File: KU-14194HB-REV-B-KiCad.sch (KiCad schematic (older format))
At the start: 0 parts

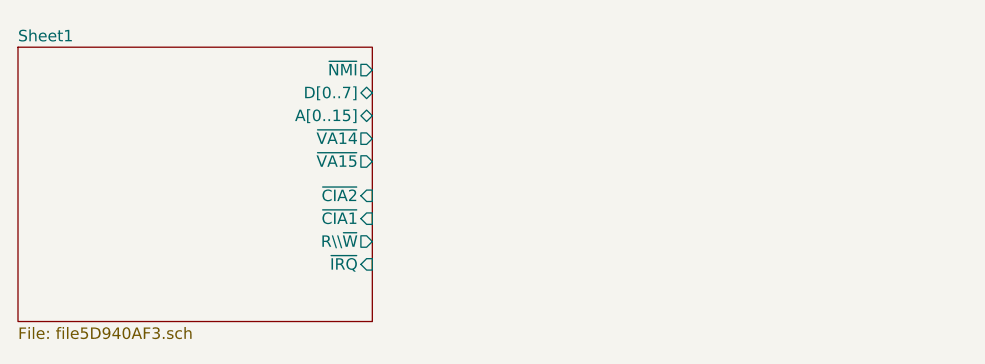
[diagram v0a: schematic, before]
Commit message: schematics update
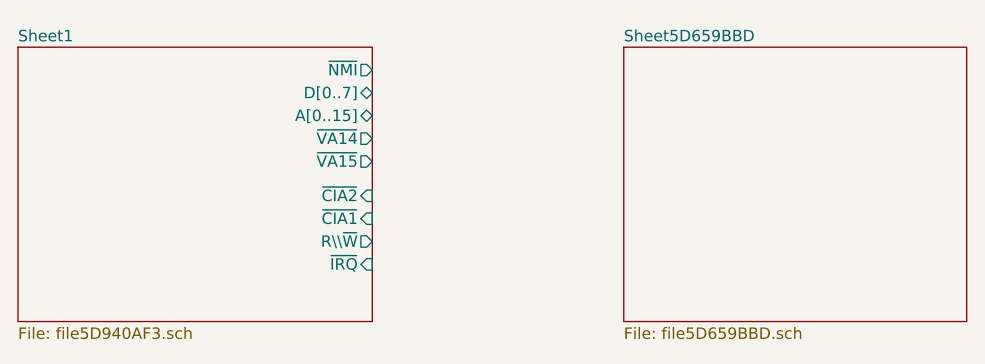
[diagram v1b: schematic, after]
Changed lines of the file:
@@
 $Descr A3 16535 11693
 encoding utf-8
-Sheet 1 2
+Sheet 1 3
 Title ""
 Date ""
@@
 F10 "~IRQ~" I R 4050 2450 50
 $EndSheet
+$Sheet
+S 5150 1500 1500 1200
+U 5D659BBE
+F0 "Sheet5D659BBD" 50
+F1 "file5D659BBD.sch" 50
+$EndSheet
 $EndSCHEMATC

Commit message: More schematics
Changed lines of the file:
@@
 F0 "Sheet5D659BBD" 50
 F1 "file5D659BBD.sch" 50
+F2 "D[0..7]" B L 5150 1700 39
 $EndSheet
+Wire Bus Line
+	5150 1700 4050 1700
+Text HLabel 4500 1700 1    39   Input ~ 0
+D[0..7]
 $EndSCHEMATC

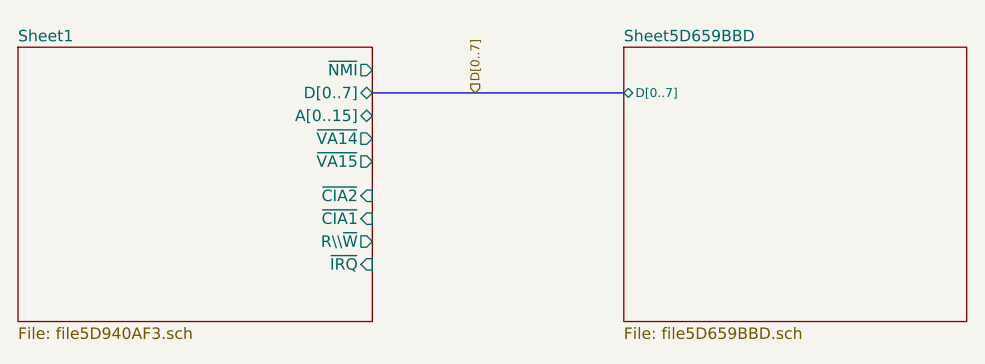
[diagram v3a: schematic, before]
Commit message: Schematics PDF and screenshot update
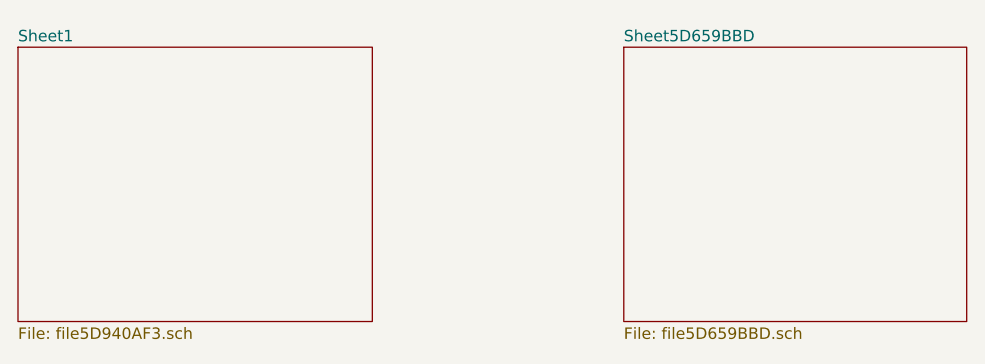
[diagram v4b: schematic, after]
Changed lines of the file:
@@
 encoding utf-8
 Sheet 1 3
-Title ""
-Date ""
+Title "C64 Motherboard KU-14194HB"
+Date "2019-09-28"
 Rev ""
-Comp ""
-Comment1 ""
+Comp "Commodore 1982"
+Comment1 "layout retraced and schematics drawn by bwack 2019"
 Comment2 ""
 Comment3 ""
@@
 F0 "Sheet1" 50
 F1 "file5D940AF3.sch" 50
-F2 "~NMI~" O R 4050 1600 50
-F3 "D[0..7]" B R 4050 1700 50
-F4 "A[0..15]" B R 4050 1800 50
-F5 "~VA14~" O R 4050 1900 50
-F6 "~VA15~" O R 4050 2000 50
-F7 "~CIA2~" I R 4050 2150 50
-F8 "~CIA1~" I R 4050 2250 50
-F9 "R\\~W~" O R 4050 2350 50
-F10 "~IRQ~" I R 4050 2450 50
 $EndSheet
 $Sheet
@@
 F0 "Sheet5D659BBD" 50
 F1 "file5D659BBD.sch" 50
-F2 "D[0..7]" B L 5150 1700 39
 $EndSheet
-Wire Bus Line
-	5150 1700 4050 1700
-Text HLabel 4500 1700 1    39   Input ~ 0
-D[0..7]
 $EndSCHEMATC
